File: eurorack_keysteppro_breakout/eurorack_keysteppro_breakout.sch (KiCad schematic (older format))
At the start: 1 part

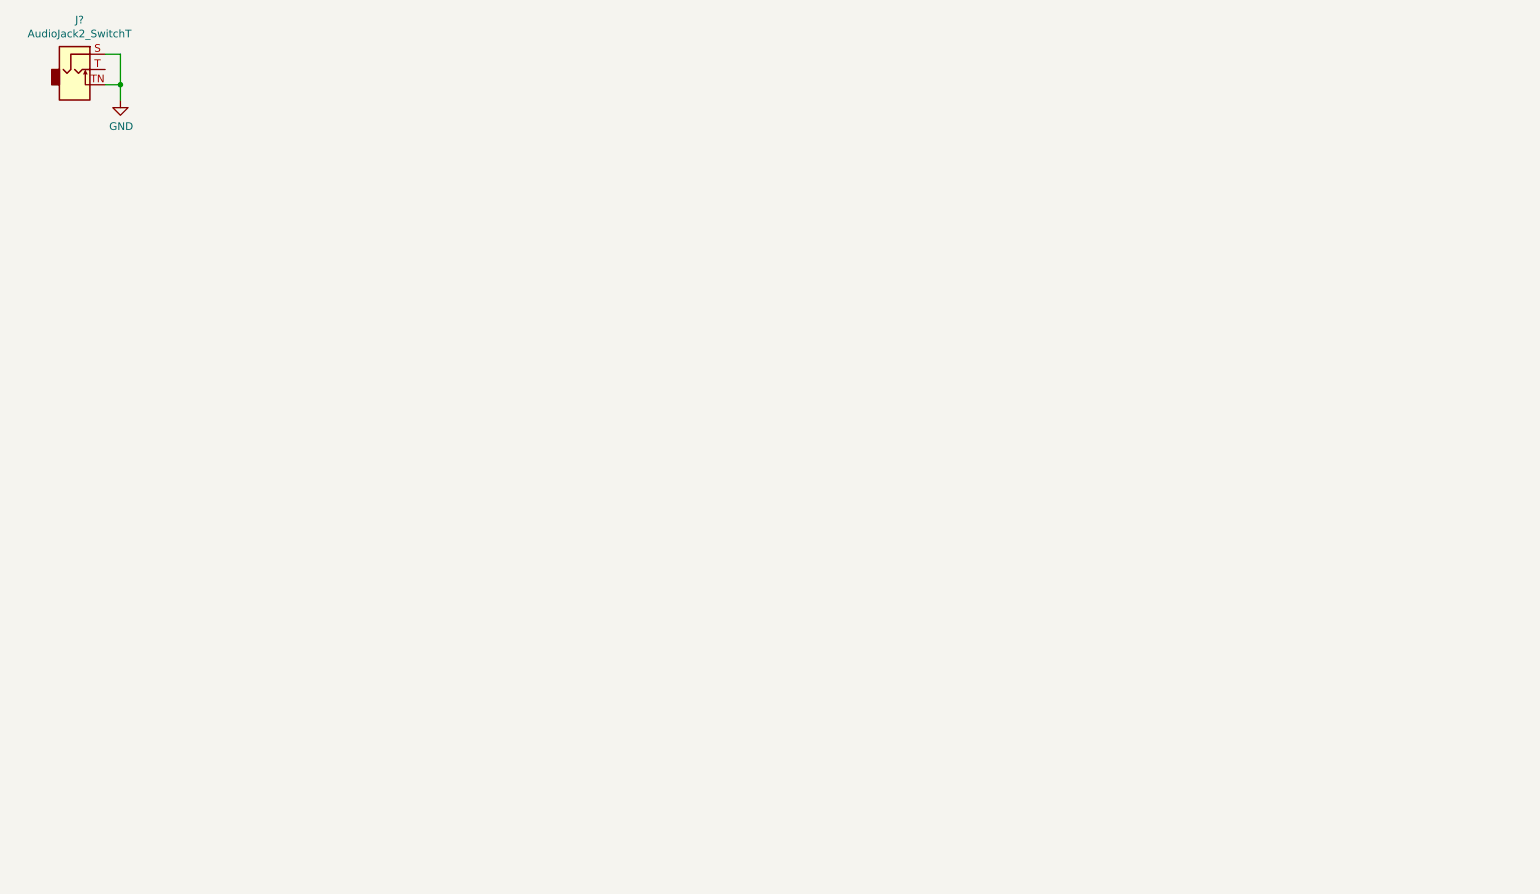
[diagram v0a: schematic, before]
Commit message: add all connectors to schema and wire stuff up
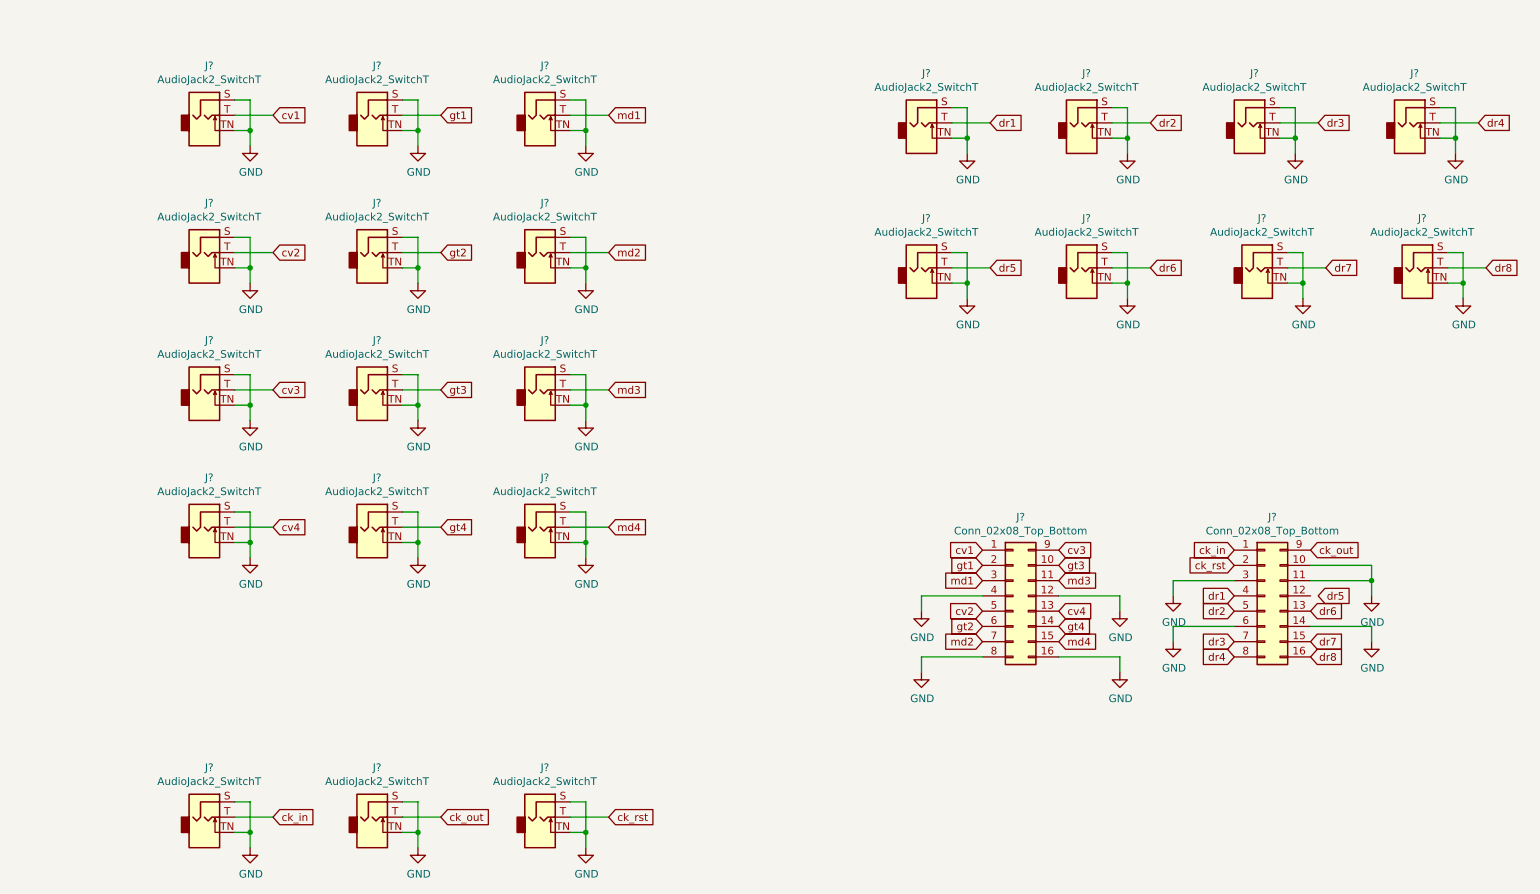
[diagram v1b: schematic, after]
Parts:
- added J? (x22): AudioJack2_SwitchT, patchnut:Jack_3.5mm_ThonkiConn_TRS-PJ366ST_Vertical, symbol Connector:AudioJack2_SwitchT
- added J? (x2): Conn_02x08_Top_Bottom, symbol Connector_Generic:Conn_02x08_Top_Bottom
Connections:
- net GND: now also J?.10 (Pin_10), J?.11 (Pin_11), J?.12 (Pin_12), J?.14 (Pin_14), J?.16 (Pin_16), J?.3 (Pin_3), J?.4 (Pin_4), J?.6 (Pin_6), J?.8 (Pin_8), J?.S, J?.S, J?.S, J?.S, J?.S, J?.S, J?.S, J?.S, J?.S, J?.S, J?.S, J?.S, J?.S, J?.S, J?.S, J?.S, J?.S, J?.S, J?.S, J?.S, J?.S, J?.S, J?.TN, J?.TN, J?.TN, J?.TN, J?.TN, J?.TN, J?.TN, J?.TN, J?.TN, J?.TN, J?.TN, J?.TN, J?.TN, J?.TN, J?.TN, J?.TN, J?.TN, J?.TN, J?.TN, J?.TN, J?.TN, J?.TN
- net cv1: now reaches J?.T
- net cv1: now also J?.1 (Pin_1)
- new net ck_in: J?.1 (Pin_1), J?.T
- new net ck_out: J?.9 (Pin_9), J?.T
- new net ck_rst: J?.2 (Pin_2), J?.T
- new net cv2: J?.5 (Pin_5), J?.T
- new net cv3: J?.9 (Pin_9), J?.T
- new net cv4: J?.13 (Pin_13), J?.T
- new net dr1: J?.4 (Pin_4), J?.T
- new net dr2: J?.5 (Pin_5), J?.T
- new net dr3: J?.7 (Pin_7), J?.T
- new net dr4: J?.8 (Pin_8), J?.T
- new net dr5: J?.T
- new net dr6: J?.13 (Pin_13), J?.T
- new net dr7: J?.15 (Pin_15), J?.T
- new net dr8: J?.16 (Pin_16), J?.T
- new net gt1: J?.2 (Pin_2), J?.T
- new net gt2: J?.6 (Pin_6), J?.T
- new net gt3: J?.10 (Pin_10), J?.T
- new net gt4: J?.14 (Pin_14), J?.T
- new net md1: J?.3 (Pin_3), J?.T
- new net md2: J?.7 (Pin_7), J?.T
- new net md3: J?.11 (Pin_11), J?.T
- new net md4: J?.15 (Pin_15), J?.T
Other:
- moved on the sheet: J?

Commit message: annotate and fix some rules checker issues
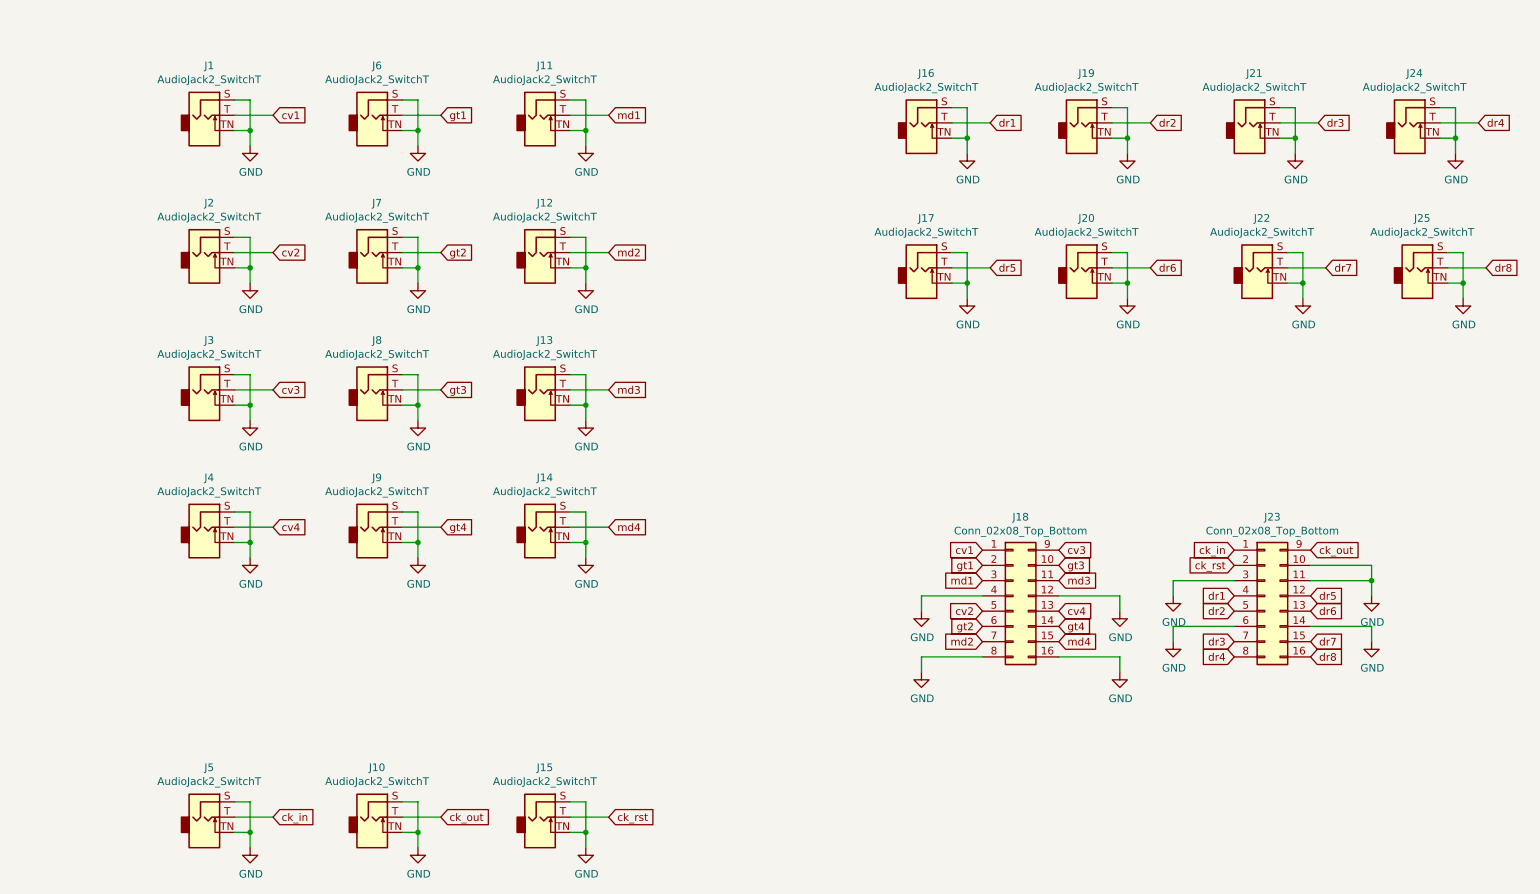
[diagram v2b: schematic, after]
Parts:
- gave numbers to parts that had none: 25
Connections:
- net dr5: now also J23.12 (Pin_12)

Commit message: fix audio jack footprints
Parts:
- J1, J10, J11, J12, J13, J14, J15, J16, J17, J19, J2, J20, J21, J22, J24, J25, J3, J4, J5, J6, J7, J8, J9: footprint patchnut:Jack_3.5mm_ThonkiConn_TRS-PJ366ST_Vertical -> Connector_Audio:Jack_3.5mm_QingPu_WQP-PJ398SM_Vertical_CircularHoles
- J18, J23: footprint (none) -> Connector_PinSocket_2.54mm:PinSocket_2x08_P2.54mm_Vertical

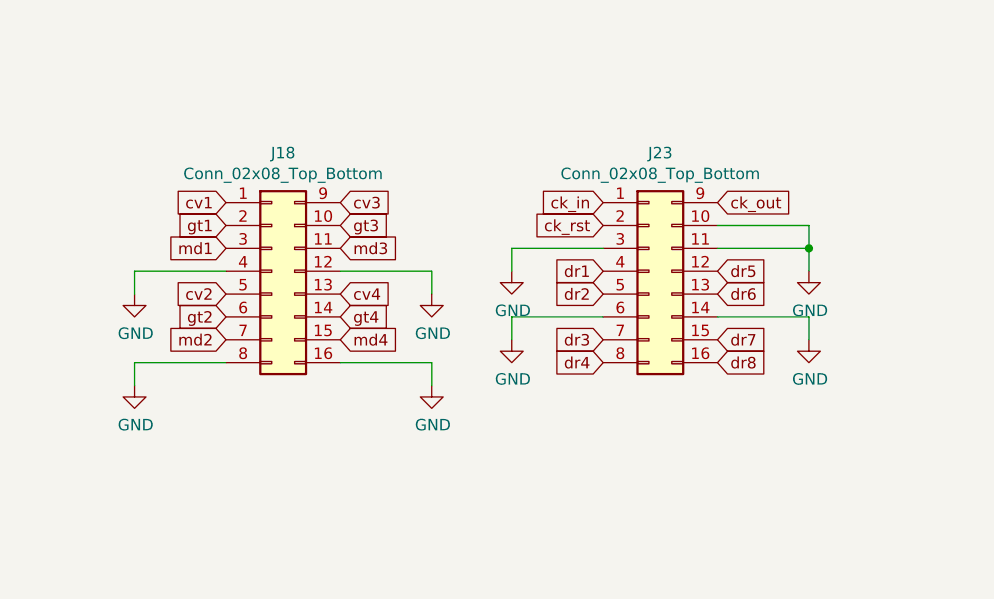
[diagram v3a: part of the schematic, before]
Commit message: fix pinheaders, flip to backside board
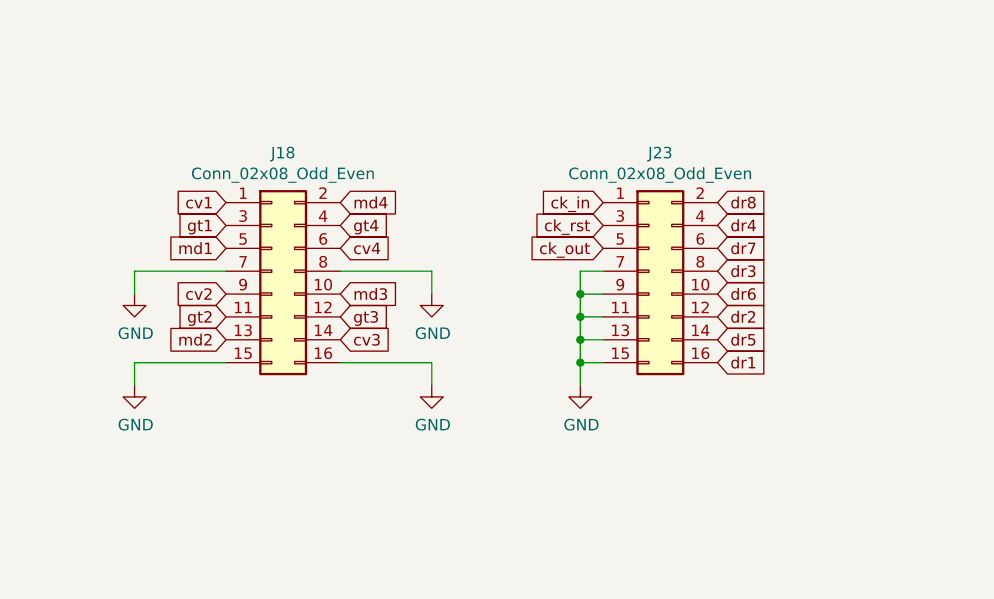
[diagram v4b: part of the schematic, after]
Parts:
- removed J18, J23: Conn_02x08_Top_Bottom, Connector_PinSocket_2.54mm:PinSocket_2x08_P2.54mm_Vertical, symbol Connector_Generic:Conn_02x08_Top_Bottom
- added J18, J23: Conn_02x08_Odd_Even, Connector_PinHeader_2.54mm:PinHeader_2x08_P2.54mm_Vertical, symbol Connector_Generic:Conn_02x08_Odd_Even
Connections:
- net GND: now also J18.15 (Pin_15), J18.16 (Pin_16), J18.7 (Pin_7), J18.8 (Pin_8), J23.11 (Pin_11), J23.13 (Pin_13), J23.15 (Pin_15), J23.7 (Pin_7), J23.9 (Pin_9)
- net ck_in: now also J23.1 (Pin_1)
- net ck_out: now also J23.5 (Pin_5)
- net ck_rst: now also J23.3 (Pin_3)
- net cv1: now also J18.1 (Pin_1)
- net cv2: now also J18.9 (Pin_9)
- net cv3: now also J18.14 (Pin_14)
- net cv4: now also J18.6 (Pin_6)
- net dr1: now also J23.16 (Pin_16)
- net dr2: now also J23.12 (Pin_12)
- net dr3: now also J23.8 (Pin_8)
- net dr4: now also J23.4 (Pin_4)
- net dr5: now also J23.14 (Pin_14)
- net dr6: now also J23.10 (Pin_10)
- net dr7: now also J23.6 (Pin_6)
- net dr8: now also J23.2 (Pin_2)
- net gt1: now also J18.3 (Pin_3)
- net gt2: now also J18.11 (Pin_11)
- net gt3: now also J18.12 (Pin_12)
- net gt4: now also J18.4 (Pin_4)
- net md1: now also J18.5 (Pin_5)
- net md2: now also J18.13 (Pin_13)
- net md3: now also J18.10 (Pin_10)
- net md4: now also J18.2 (Pin_2)
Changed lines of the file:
@@
 	8000 1500 8250 1500
 $Comp
-L power:GND #PWR026
+L power:GND #PWR025
 U 1 1 619D3DDE
 P 9200 1700
-F 0 "#PWR026" H 9200 1450 50  0001 C CNN
+F 0 "#PWR025" H 9200 1450 50  0001 C CNN
 F 1 "GND" H 9205 1527 50  0000 C CNN
 F 2 "" H 9200 1700 50  0001 C CNN
@@
 	9100 1500 9350 1500
 $Comp
-L power:GND #PWR030
+L power:GND #PWR027
 U 1 1 619D3DF1
 P 10250 1700
-F 0 "#PWR030" H 10250 1450 50  0001 C CNN
+F 0 "#PWR027" H 10250 1450 50  0001 C CNN
 F 1 "GND" H 10255 1527 50  0000 C CNN
 F 2 "" H 10250 1700 50  0001 C CNN
@@
 	10150 1500 10400 1500
 $Comp
-L power:GND #PWR027
+L power:GND #PWR026
 U 1 1 619D6D66
 P 9250 2650
-F 0 "#PWR027" H 9250 2400 50  0001 C CNN
+F 0 "#PWR026" H 9250 2400 50  0001 C CNN
 F 1 "GND" H 9255 2477 50  0000 C CNN
 F 2 "" H 9250 2650 50  0001 C CNN
@@
 	9150 2450 9400 2450
 $Comp
-L power:GND #PWR031
+L power:GND #PWR028
 U 1 1 619D6D79
 P 10300 2650
-F 0 "#PWR031" H 10300 2400 50  0001 C CNN
+F 0 "#PWR028" H 10300 2400 50  0001 C CNN
 F 1 "GND" H 10305 2477 50  0000 C CNN
 F 2 "" H 10300 2650 50  0001 C CNN
@@
 Wire Wire Line
 	4450 6050 4700 6050
-$Comp
-L Connector_Generic:Conn_02x08_Top_Bottom J18
-U 1 1 61A4395F
-P 7350 4600
-F 0 "J18" H 7400 5117 50  0000 C CNN
-F 1 "Conn_02x08_Top_Bottom" H 7400 5026 50  0000 C CNN
-F 2 "Connector_PinSocket_2.54mm:PinSocket_2x08_P2.54mm_Vertical" H 7350 4600 50  0001 C CNN
-F 3 "~" H 7350 4600 50  0001 C CNN
-	1    7350 4600
-	1    0    0    -1
-$EndComp
 Text GLabel 7150 4300 0    50   Input ~ 0
 cv1
@@
 Text GLabel 7150 4900 0    50   Input ~ 0
 md2
+Text GLabel 7650 4900 2    50   Input ~ 0
+cv3
+Text GLabel 7650 4800 2    50   Input ~ 0
+gt3
+Text GLabel 7650 4700 2    50   Input ~ 0
+md3
+Text GLabel 7650 4500 2    50   Input ~ 0
+cv4
+Text GLabel 7650 4400 2    50   Input ~ 0
+gt4
 Text GLabel 7650 4300 2    50   Input ~ 0
-cv3
-Text GLabel 7650 4400 2    50   Input ~ 0
-gt3
-Text GLabel 7650 4500 2    50   Input ~ 0
-md3
-Text GLabel 7650 4700 2    50   Input ~ 0
-cv4
-Text GLabel 7650 4800 2    50   Input ~ 0
-gt4
-Text GLabel 7650 4900 2    50   Input ~ 0
 md4
 Text GLabel 8800 4300 0    50   Input ~ 0
 ck_in
-Text GLabel 9300 4300 2    50   Input ~ 0
+Text GLabel 8800 4500 0    50   Input ~ 0
 ck_out
 Text GLabel 8800 4400 0    50   Input ~ 0
 ck_rst
-Text GLabel 8800 4600 0    50   Input ~ 0
+Text GLabel 9300 5000 2    50   Input ~ 0
 dr1
-Text GLabel 8800 4700 0    50   Input ~ 0
+Text GLabel 9300 4800 2    50   Input ~ 0
 dr2
-Text GLabel 8800 4900 0    50   Input ~ 0
+Text GLabel 9300 4600 2    50   Input ~ 0
 dr3
-Text GLabel 8800 5000 0    50   Input ~ 0
+Text GLabel 9300 4400 2    50   Input ~ 0
 dr4
-$Comp
-L Connector_Generic:Conn_02x08_Top_Bottom J23
-U 1 1 61A4479A
-P 9000 4600
-F 0 "J23" H 9050 5117 50  0000 C CNN
-F 1 "Conn_02x08_Top_Bottom" H 9050 5026 50  0000 C CNN
-F 2 "Connector_PinSocket_2.54mm:PinSocket_2x08_P2.54mm_Vertical" H 9000 4600 50  0001 C CNN
-F 3 "~" H 9000 4600 50  0001 C CNN
-	1    9000 4600
-	1    0    0    -1
-$EndComp
-Text GLabel 9300 4600 2    50   Input ~ 0
+Text GLabel 9300 4900 2    50   Input ~ 0
 dr5
 Text GLabel 9300 4700 2    50   Input ~ 0
 dr6
-Text GLabel 9300 4900 2    50   Input ~ 0
+Text GLabel 9300 4500 2    50   Input ~ 0
 dr7
-Text GLabel 9300 5000 2    50   Input ~ 0
+Text GLabel 9300 4300 2    50   Input ~ 0
 dr8
 $Comp
@@
 	8050 5000 8050 5100
 $Comp
-L power:GND #PWR025
+L power:GND #PWR024
 U 1 1 61A7AB11
-P 8400 4900
-F 0 "#PWR025" H 8400 4650 50  0001 C CNN
-F 1 "GND" H 8405 4727 50  0000 C CNN
-F 2 "" H 8400 4900 50  0001 C CNN
-F 3 "" H 8400 4900 50  0001 C CNN
-	1    8400 4900
-	1    0    0    -1
-$EndComp
-$Comp
-L power:GND #PWR024
-U 1 1 61A7BC62
-P 8400 4600
-F 0 "#PWR024" H 8400 4350 50  0001 C CNN
-F 1 "GND" H 8405 4427 50  0000 C CNN
-F 2 "" H 8400 4600 50  0001 C CNN
-F 3 "" H 8400 4600 50  0001 C CNN
-	1    8400 4600
-	1    0    0    -1
-$EndComp
-$Comp
-L power:GND #PWR028
-U 1 1 61A7C516
-P 9700 4600
-F 0 "#PWR028" H 9700 4350 50  0001 C CNN
-F 1 "GND" H 9705 4427 50  0000 C CNN
-F 2 "" H 9700 4600 50  0001 C CNN
-F 3 "" H 9700 4600 50  0001 C CNN
-	1    9700 4600
-	1    0    0    -1
-$EndComp
-$Comp
-L power:GND #PWR029
-U 1 1 61A7D05E
-P 9700 4900
-F 0 "#PWR029" H 9700 4650 50  0001 C CNN
-F 1 "GND" H 9705 4727 50  0000 C CNN
-F 2 "" H 9700 4900 50  0001 C CNN
-F 3 "" H 9700 4900 50  0001 C CNN
-	1    9700 4900
-	1    0    0    -1
-$EndComp
-Wire Wire Line
-	9300 4800 9700 4800
-Wire Wire Line
-	9700 4800 9700 4900
-Wire Wire Line
-	8800 4800 8400 4800
-Wire Wire Line
-	8400 4800 8400 4900
-Wire Wire Line
-	8400 4600 8400 4500
-Wire Wire Line
-	8400 4500 8800 4500
-Wire Wire Line
-	9300 4400 9700 4400
-Wire Wire Line
-	9700 4400 9700 4500
-Wire Wire Line
-	9300 4500 9700 4500
-Connection ~ 9700 4500
-Wire Wire Line
-	9700 4500 9700 4600
+P 8700 5100
+F 0 "#PWR024" H 8700 4850 50  0001 C CNN
+F 1 "GND" H 8705 4927 50  0000 C CNN
+F 2 "" H 8700 5100 50  0001 C CNN
+F 3 "" H 8700 5100 50  0001 C CNN
+	1    8700 5100
+	1    0    0    -1
+$EndComp
 $Comp
 L Connector:AudioJack2_SwitchT J2
@@
 	1    0    0    -1
 $EndComp
+$Comp
+L Connector_Generic:Conn_02x08_Odd_Even J18
+U 1 1 61AE442C
+P 7350 4600
+F 0 "J18" H 7400 5117 50  0000 C CNN
+F 1 "Conn_02x08_Odd_Even" H 7400 5026 50  0000 C CNN
+F 2 "Connector_PinHeader_2.54mm:PinHeader_2x08_P2.54mm_Vertical" H 7350 4600 50  0001 C CNN
+F 3 "~" H 7350 4600 50  0001 C CNN
+	1    7350 4600
+	1    0    0    -1
+$EndComp
+$Comp
+L Connector_Generic:Conn_02x08_Odd_Even J23
+U 1 1 61AE5894
+P 9000 4600
+F 0 "J23" H 9050 5117 50  0000 C CNN
+F 1 "Conn_02x08_Odd_Even" H 9050 5026 50  0000 C CNN
+F 2 "Connector_PinHeader_2.54mm:PinHeader_2x08_P2.54mm_Vertical" H 9000 4600 50  0001 C CNN
+F 3 "~" H 9000 4600 50  0001 C CNN
+	1    9000 4600
+	1    0    0    -1
+$EndComp
+Wire Wire Line
+	8800 4600 8700 4600
+Wire Wire Line
+	8700 4600 8700 4700
+Wire Wire Line
+	8800 4700 8700 4700
+Connection ~ 8700 4700
+Wire Wire Line
+	8700 4700 8700 4800
+Wire Wire Line
+	8800 4800 8700 4800
+Connection ~ 8700 4800
+Wire Wire Line
+	8700 4800 8700 4900
+Wire Wire Line
+	8800 4900 8700 4900
+Connection ~ 8700 4900
+Wire Wire Line
+	8700 4900 8700 5000
+Wire Wire Line
+	8800 5000 8700 5000
+Connection ~ 8700 5000
+Wire Wire Line
+	8700 5000 8700 5100
 $EndSCHEMATC
